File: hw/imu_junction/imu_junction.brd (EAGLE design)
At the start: 62 x 44 mm, 58 parts, among them J1 JST-PH3SMT_VERT, J2 JST-PH3SMT_VERT, J3 JST-PH3SMT_VERT, J4 JST-PH3SMT_VERT, J5 JST-XH4SMT_RA, U1 STM32F4R_64PIN, U2 BMI088LGA16, U3 TPS62177WSON10, U4 MAX13431E, U5 MAX13431E, U6 MAX13431E, X1 8.0MHz

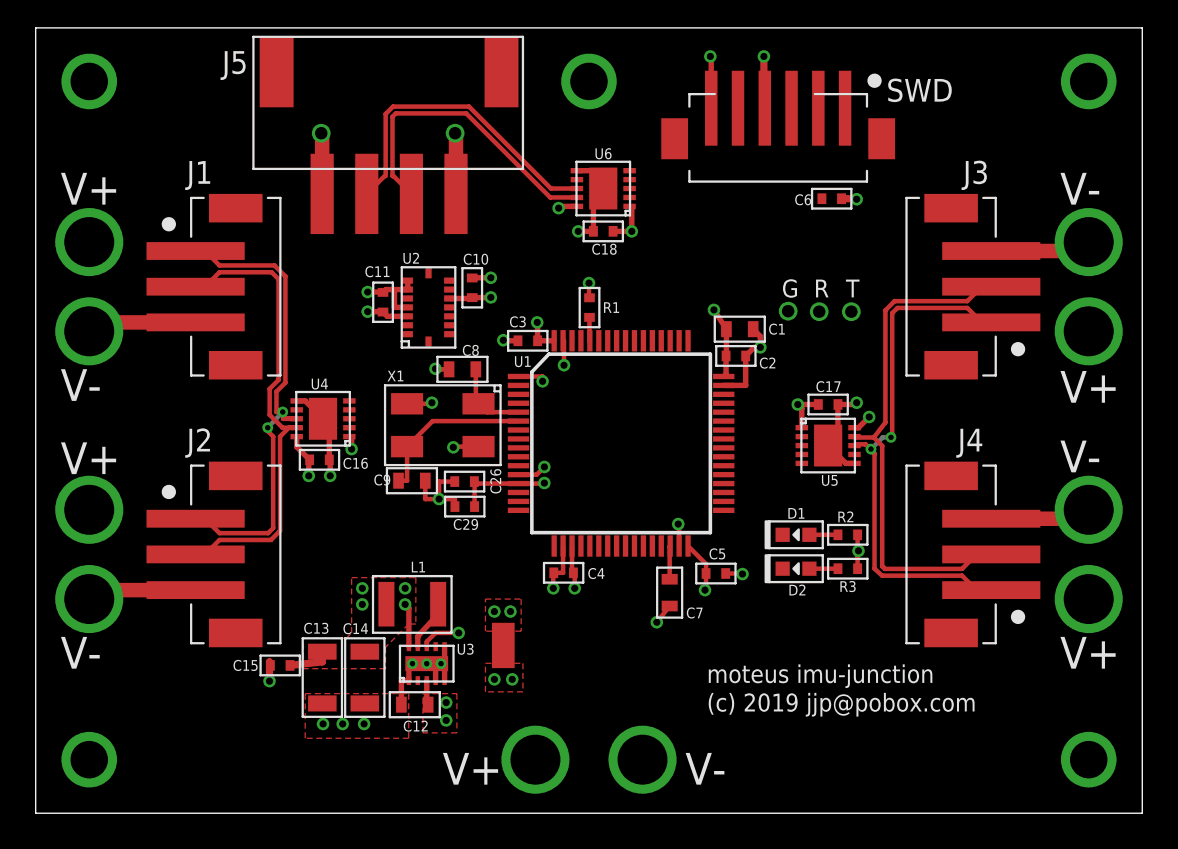
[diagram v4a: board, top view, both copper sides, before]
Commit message: imu_junction: Route and refine silks
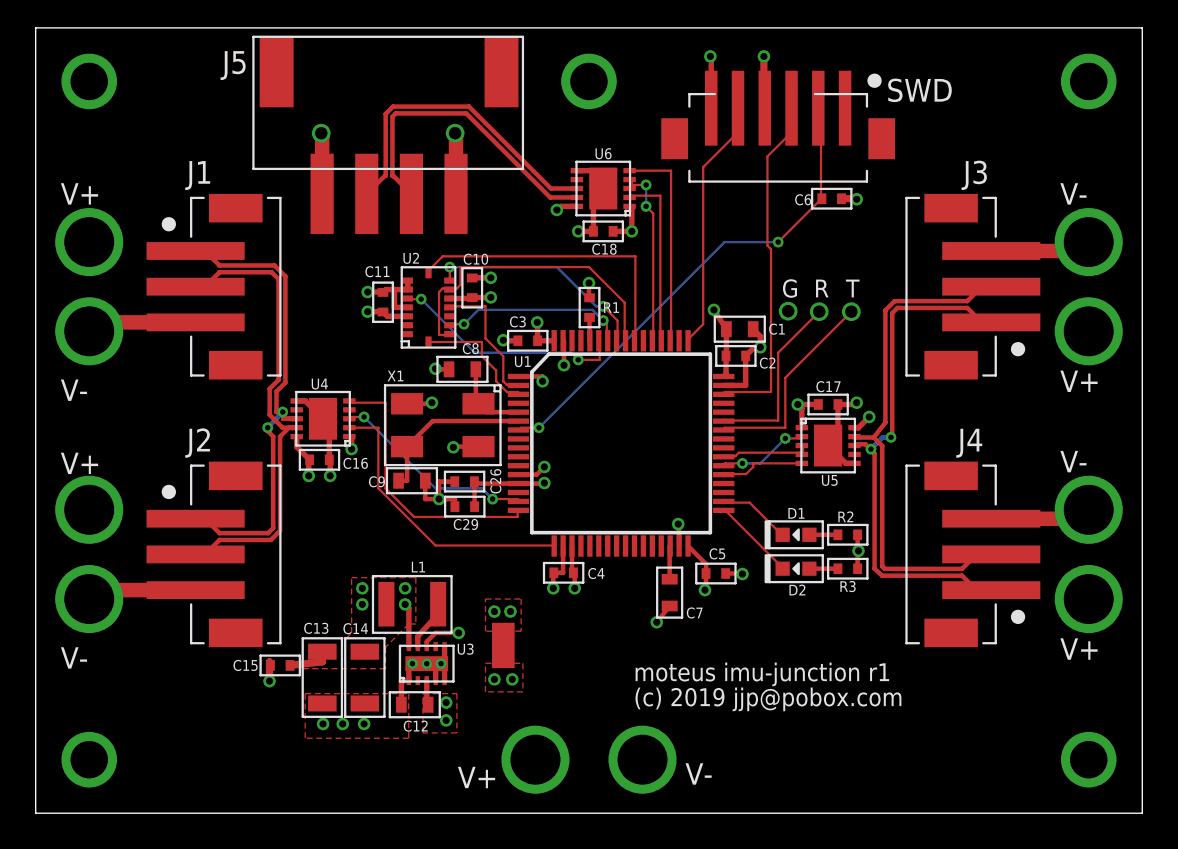
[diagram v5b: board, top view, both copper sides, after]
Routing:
- net N$24: track 0.00 -> 27.5 mm, vias 0 -> 2
- net N$7: track 0.00 -> 19.3 mm
- net IMU_MISO: track 0.00 -> 17.6 mm
- net IMU_SCK: track 0.00 -> 16.8 mm
- net RX1: track 0.00 -> 16.2 mm
- net TX1: track 0.00 -> 15.4 mm
- net N$6: track 0.00 -> 14.2 mm
- net IMU_CS2: track 0.00 -> 13.2 mm, vias 0 -> 2
- net IMU_MOSI: track 0.00 -> 12.5 mm, vias 0 -> 2
- net DIR1: track 0.00 -> 12.0 mm, vias 0 -> 2
- net TX3: track 0.00 -> 11.9 mm
- net N$2: track 0.00 -> 11.6 mm
- net IMU_CS1: track 0.00 -> 10.5 mm, vias 0 -> 2
- net DIR3: track 0.00 -> 10.4 mm, vias 0 -> 2
- net N$3: track 0.00 -> 10.1 mm
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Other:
- board text added: "moteus imu-junction r1"
- board text removed: "moteus imu-junction"

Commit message: imu_junction r2
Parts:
- removed U$5: MOUNTM2, controller:M2MOUNT
- added C19: 10uF 35V, mfpassives:C1206
- added F1, F2: JST-PH2, imu_junction:JST_S2B-PH-SM4-TB(LF)(SN)
- added U7, U8: MF-DSC-SOT233-BSS138, mfdiscretesemi:SOT-23-3
- C12: value 2.2uF 35V -> 10uF 35V; device mfpassives:C0603 -> mfpassives:C1206
- C13, C14: value 10uF -> 10uF 35V
- moved C12 3.17 mm to (22.0, 3.00)
- moved C17 2.80 mm to (44.5, 25.7)
- moved D2 2.80 mm to (42.7, 16.5)
- moved J4 2.80 mm to (51.1, 17.3)
- moved R3 2.80 mm to (45.6, 16.5)
- moved V+3 2.80 mm to (59.1, 29.8)
- moved V+4 2.80 mm to (59.1, 14.8)
- moved V-4 2.80 mm to (59.1, 19.8)
- moved D1 2.80 mm to (42.7, 18.4)
- moved R2 2.80 mm to (45.6, 18.4)
- moved J3 2.80 mm to (51.1, 32.3)
- moved U5 2.80 mm to (44.5, 23.4)
- moved V-3 2.80 mm to (59.1, 34.8)
- moved C16 2.80 mm to (15.9, 22.6)
- moved J2 2.80 mm to (11.5, 17.3)
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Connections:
- new net FAN1: U1.22, U7.P$1
- new net FAN2: U1.23, U8.P$1
- new net N$4: F1.2, U7.P$3
- new net N$9: F2.2, U8.P$3
- net +18V: now also C19.P$1, F1.1, F2.1
- net V-: now also C19.P$2, U7.P$2, U8.P$2
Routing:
- net FAN2: track 0.00 -> 21.4 mm
- net DIR2: track 5.10 -> 18.2 mm
- net FAN1: track 0.00 -> 7.19 mm
- net N$4: track 0.00 -> 7.00 mm
- net +18V: track 5.35 -> 10.0 mm, vias 3 -> 7
- net N$9: track 0.00 -> 4.01 mm
- net V-: track 34.5 -> 38.3 mm, vias 7 -> 9
- net N$3: track 10.1 -> 13.8 mm, vias 0 -> 1
- net RX2: track 5.08 -> 8.02 mm, vias 2 -> 0
- net TX1: track 15.4 -> 18.2 mm
- net RX1: track 16.2 -> 19.0 mm
- net DIR1: track 12.0 -> 14.5 mm
- net TX2: track 4.75 -> 6.24 mm, vias 0 -> 2
- net N$2: track 11.6 -> 13.1 mm, vias 0 -> 1
- net STATUS2: track 4.70 -> 3.84 mm
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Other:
- board text added: "moteus imu-junction r2"
- board text removed: "moteus imu-junction r1"

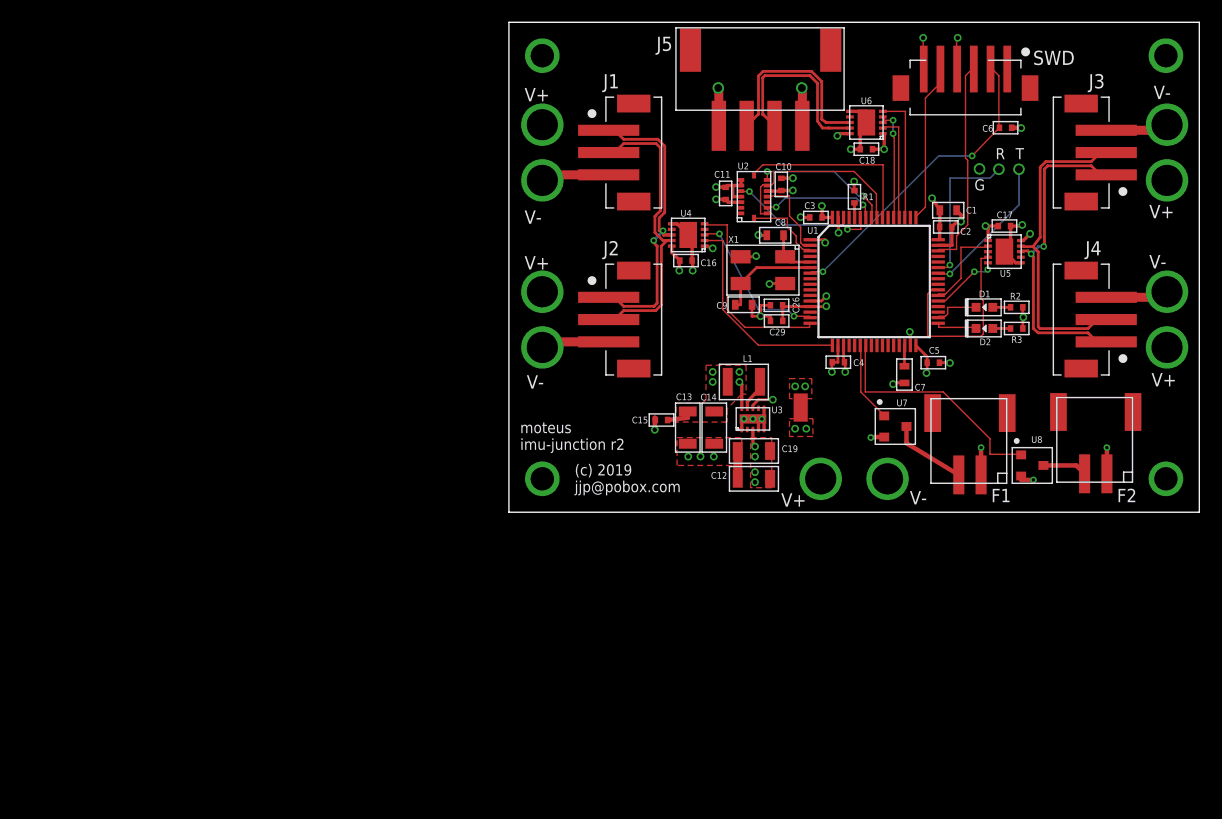
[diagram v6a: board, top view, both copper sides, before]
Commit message: Work towards an r3 of the imu junction board
Decided that I can probably live for now with just an anti-spark
connector on the battery.  I hadn't decided how to handle the common
mode ground shift on the RS485 bus with a switched ground system
during the startup transient.
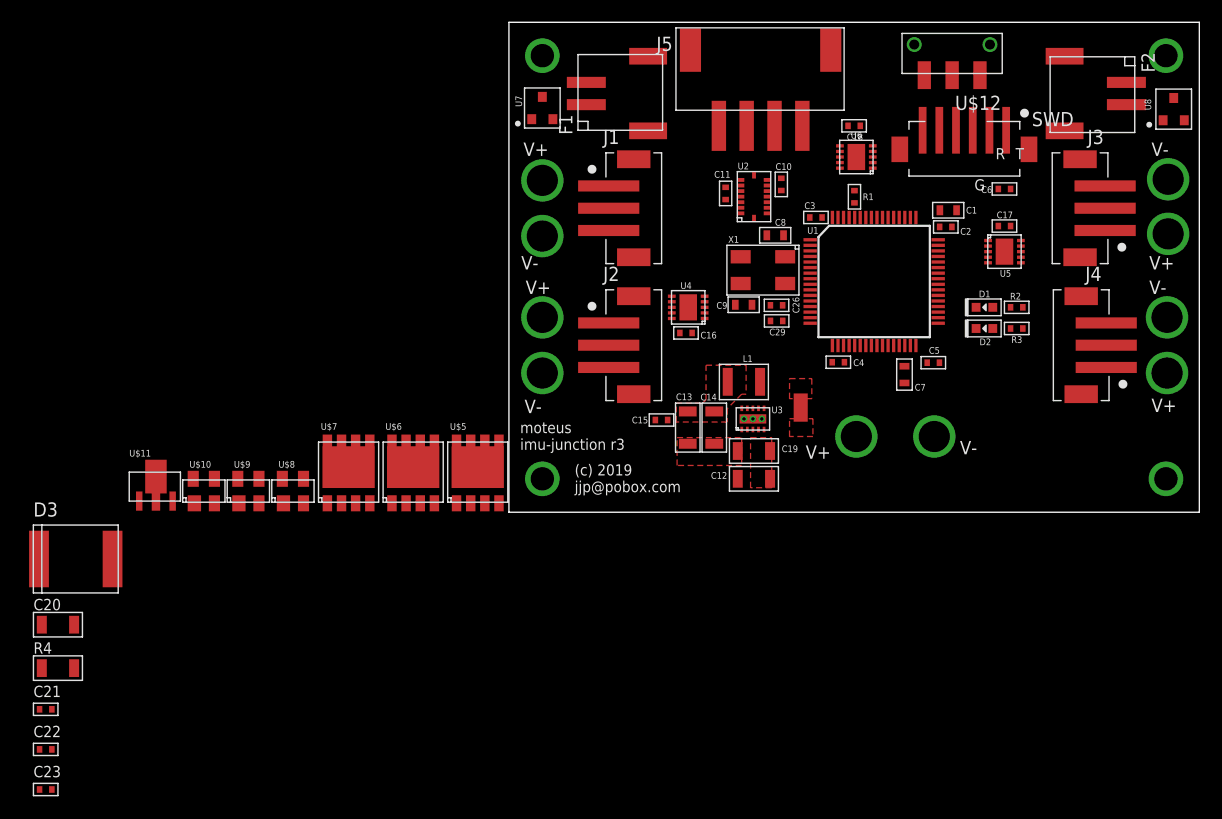
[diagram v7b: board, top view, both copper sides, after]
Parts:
- removed DGND, DRX, DTX: PAD24AWG_PAD, controller:24AWG_PAD
- added C20: 10uF 35V, mfpassives:C1206
- added C21, C22, C23: 0.1uF 50V, mfpassives:C0402
- added D3: (no value), imu_junction:DO-214AB
- added R4: 10 1W, mfpassives:R1206
- added U$10, U$8, U$9: MIC4416, imu_junction:SOT143
- added U$11: ZXTR2012Z, imu_junction:SOT89
- added U$12: SLIDE_SWITCHJS_SUB_SWITCH, imu_junction:JS_SUB_SWITCH
- added U$5, U$6, U$7: TPH1R204PL, imu_junction:SOP_ADVANCE
- moved F1 44.8 mm to (9.60, 37.6), turned to 270 degrees
- moved U7 42.7 mm to (3.00, 36.3), turned to 90 degrees
- moved U8 34.4 mm to (59.7, 36.2), turned to 90 degrees
- moved F2 31.5 mm to (52.8, 37.6), turned to 90 degrees
- moved C16 6.50 mm to (15.9, 16.1)
- moved U4 6.50 mm to (16.1, 18.4)
- moved V- 5.66 mm to (38.2, 6.80)
- moved C6 5.50 mm to (44.5, 29.0)
- moved SWD 5.50 mm to (40.9, 32.3)
- moved J3 5.00 mm to (51.0, 27.3)
- moved V-1 5.00 mm to (3.00, 24.8)
- moved J1 5.00 mm to (11.5, 27.3)
- moved V+1 5.00 mm to (3.00, 29.8)
- moved V+ 4.97 mm to (31.2, 6.80)
- moved V-3 4.90 mm to (59.2, 29.9)
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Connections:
- removed net N$3: DRX.P$1, U1.43
- new net +12V: C20.P$1, C21.P$1, C22.P$1, C23.P$1, U$10.3, U$11.3, U$8.3, U$9.3
- new net N$10: R4.P$1, U$5.5, U$5.6, U$5.7, U$5.8, U$5.PAD
- new net N$11: U$6.4, U$9.2
- new net N$12: U$5.4, U$8.2
- new net N$13: U$10.2, U$7.4
- new net PWR_CPU: U$10.4
- new net PWR_MOTOR: U$9.4
- new net PWR_PRECHARGE: U$8.4
- new net V-CPU: J5.1, U$7.5, U$7.6, U$7.7, U$7.8, U$7.PAD
- new net V-MOTOR: D3.A, J1.3, J2.3, J3.3, J4.3, R4.P$2, U$6.5, U$6.6, U$6.7, U$6.8, U$6.PAD
- net +18V: now also D3.C, U$11.2, U$11.PAD
- net GND: now also C20.P$2, C21.P$2, C22.P$2, C23.P$2, U$10.1, U$11.1, U$12.3, U$8.1, U$9.1; no longer DGND.P$1
- net N$2: now also U$12.2, U1.8; no longer DTX.P$1, U1.42
- net V-: now also U$5.1, U$5.2, U$5.3, U$6.1, U$6.2, U$6.3, U$7.1, U$7.2, U$7.3; no longer J1.3, J2.3, J3.3, J4.3, J5.1
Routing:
- net GND: track 50.8 -> 0.00 mm, vias 22 -> 0
- net +3V3: track 45.8 -> 0.00 mm, vias 21 -> 0
- net V-: track 38.3 -> 0.00 mm, vias 9 -> 0
- net D2_P: track 29.6 -> 0.00 mm, vias 2 -> 0
- net D2_N: track 28.8 -> 0.00 mm
- net N$24: track 28.1 -> 0.00 mm, vias 2 -> 0
- net D1_P: track 27.8 -> 0.00 mm, vias 2 -> 0
- net D1_N: track 26.5 -> 0.00 mm
- net FAN2: track 21.4 -> 0.00 mm
- net RX1: track 19.0 -> 0.00 mm
- net N$7: track 18.8 -> 0.00 mm
- net TX1: track 18.2 -> 0.00 mm
- net DIR2: track 18.2 -> 0.00 mm
- net IMU_MISO: track 17.6 -> 0.00 mm
- net D3_P: track 17.2 -> 0.00 mm
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- removed copper zone on layer 2, net V-
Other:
- board text added: "moteus imu-junction r3"
- board text removed: "moteus imu-junction r2"
